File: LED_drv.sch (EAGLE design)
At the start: 42 parts, among them IC1 LM3409, IC2 LM393D, T1 IRLR9343PBF, T4 BT169, T5 BT169, T6 TLP266J

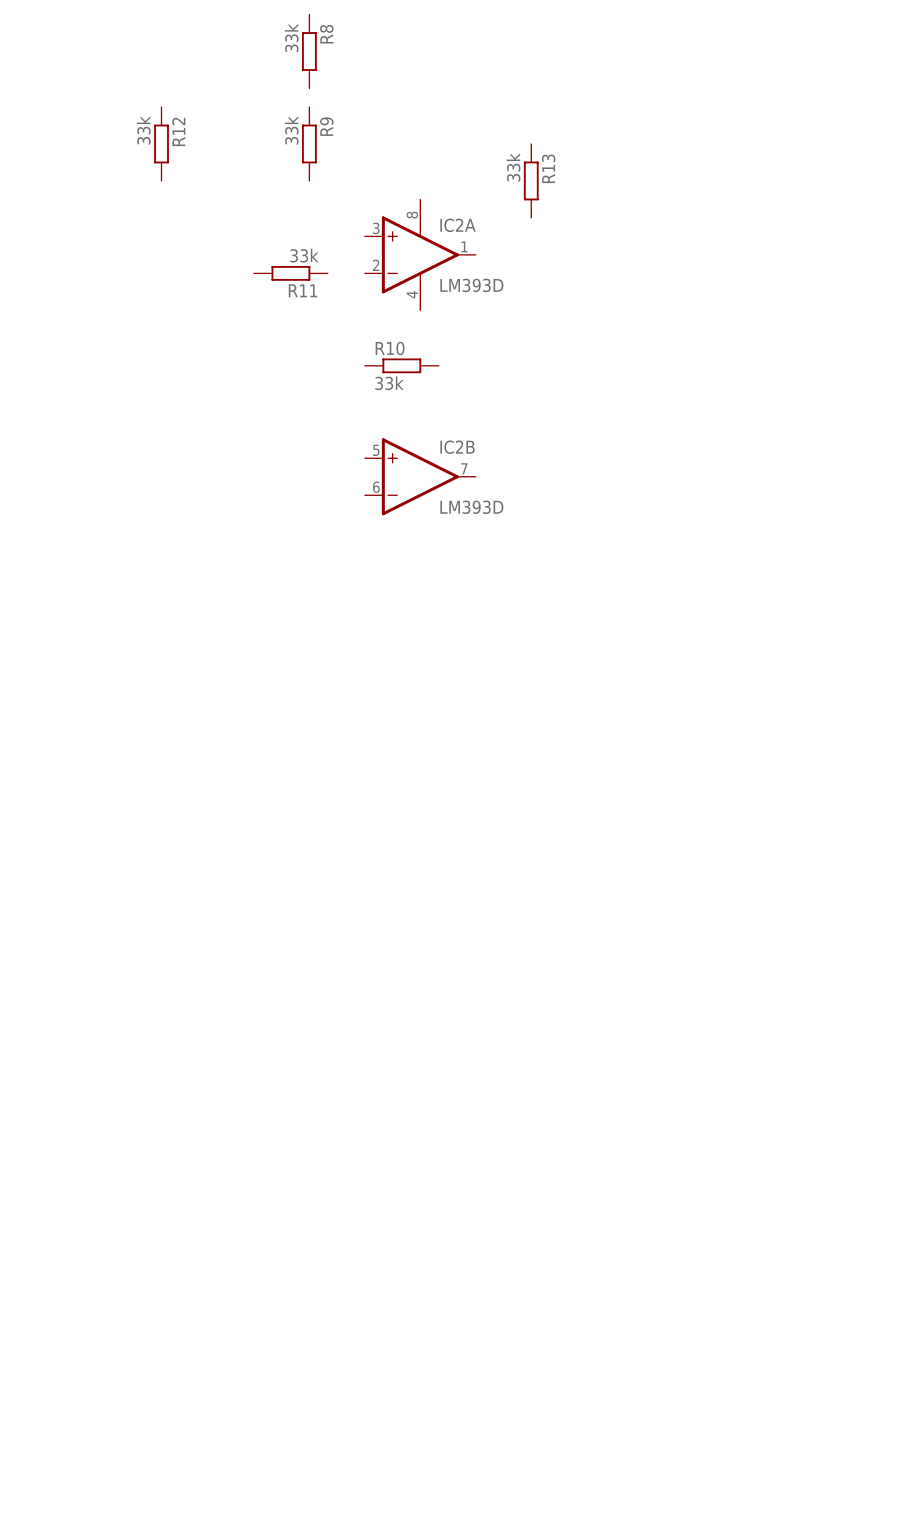
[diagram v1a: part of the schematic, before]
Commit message: Charge regeneration circuit
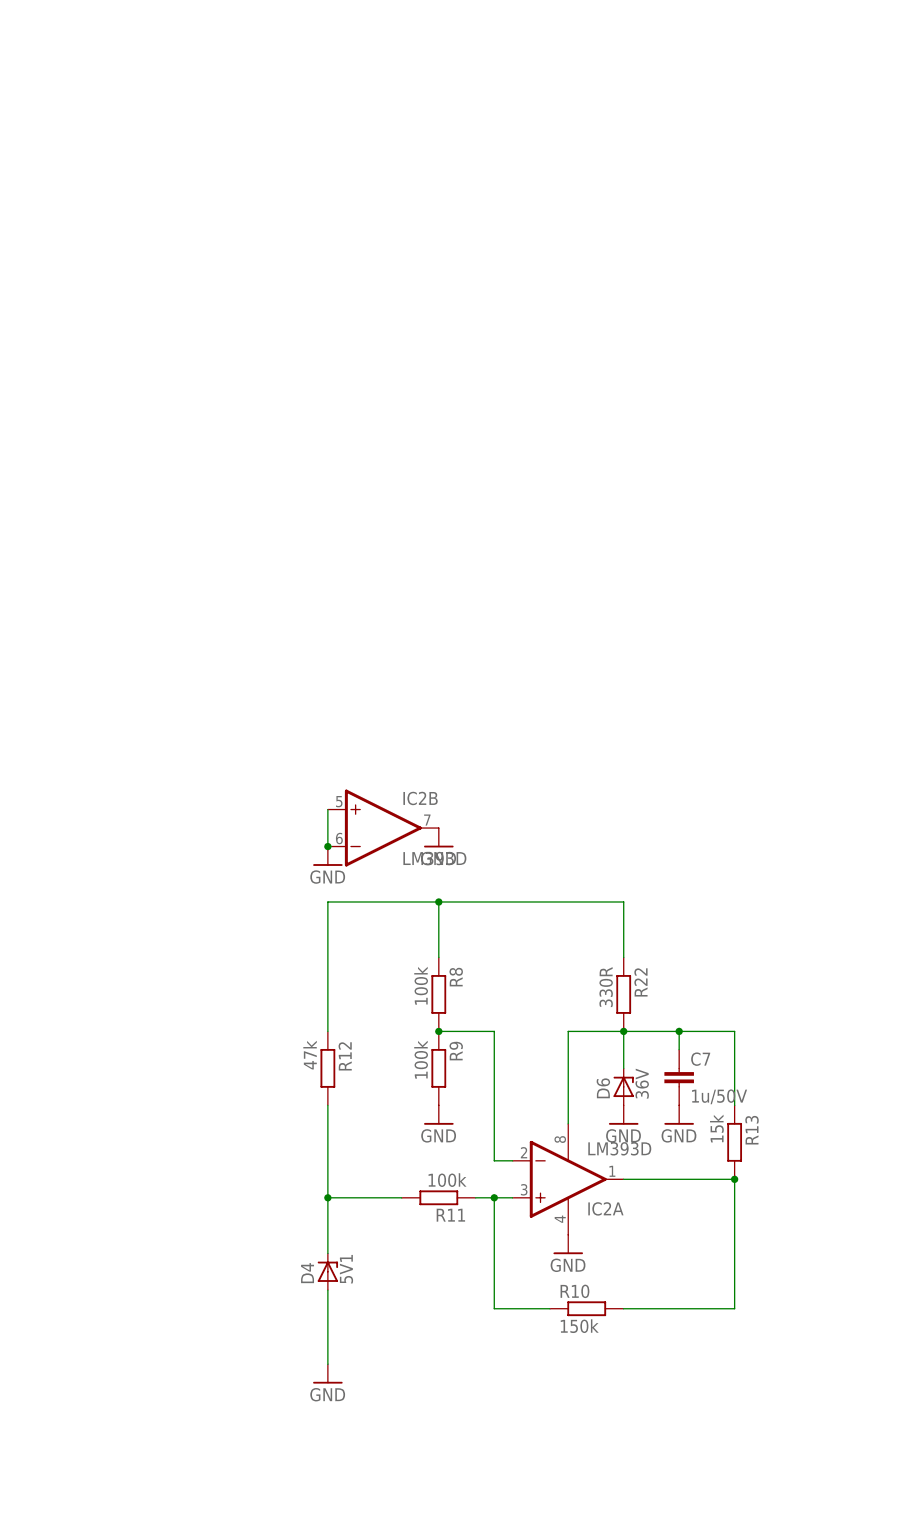
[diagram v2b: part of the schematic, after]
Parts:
- added C7: 1u/50V, rcl:C-EUC1206
- added D4: 5V1, diode:ZENER-DIODESOD80C
- added D6: 36V, diode:ZENER-DIODESOD80C
- added R22: 330R, resistor:R-EU_R0805
- R10: value 33k -> 150k
- R11, R8, R9: value 33k -> 100k
- R12: value 33k -> 47k
- R13: value 33k -> 15k
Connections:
- new net N$19: C7.1, D6.C, IC2P.V+, R13.1, R22.2
- new net N$20: IC2A.+IN, R10.1, R11.1
- new net N$21: IC2A.-IN, R8.2, R9.1
- new net N$22: D4.C, R11.2, R12.2
- new net N$27: R12.1, R22.1, R8.1
- new net N$29: IC2A.OUT, R10.2, R13.2
- net GND: now also C7.2, D4.A, D6.A, IC2B.+IN, IC2B.-IN, IC2B.OUT, IC2P.V-, R9.2
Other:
- moved on the sheet: IC2A, IC2B, R10, R11, R12, R13, R8, R9
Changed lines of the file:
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@@
 <setting verticaltext="up"/>
 </settings>
-<grid distance="0.1" unitdist="inch" unit="inch" style="lines" multiple="1" display="no" altdistance="0.05" altunitdist="inch" altunit="inch"/>
+<grid distance="0.1" unitdist="inch" unit="inch" style="lines" multiple="1" display="no" altdistance="0.01" altunitdist="inch" altunit="inch"/>
 <layers>
 <layer number="1" name="Top" color="4" fill="1" visible="no" active="no"/>
@@
 <part name="GND8" library="supply1" deviceset="GND" device=""/>
 <part name="IC2" library="linear" deviceset="LM393" device="D"/>
-<part name="R8" library="resistor" deviceset="R-EU_" device="R0805" value="33k"/>
-<part name="R9" library="resistor" deviceset="R-EU_" device="R0805" value="33k"/>
-<part name="R10" library="resistor" deviceset="R-EU_" device="R0805" value="33k"/>
-<part name="R11" library="resistor" deviceset="R-EU_" device="R0805" value="33k"/>
-<part name="R12" library="resistor" deviceset="R-EU_" device="R0805" value="33k"/>
-<part name="R13" library="resistor" deviceset="R-EU_" device="R0805" value="33k"/>
+<part name="R8" library="resistor" deviceset="R-EU_" device="R0805" value="100k"/>
+<part name="R9" library="resistor" deviceset="R-EU_" device="R0805" value="100k"/>
+<part name="R10" library="resistor" deviceset="R-EU_" device="R0805" value="150k"/>
+<part name="R11" library="resistor" deviceset="R-EU_" device="R0805" value="100k"/>
+<part name="R12" library="resistor" deviceset="R-EU_" device="R0805" value="47k"/>
 <part name="C6" library="rcl" deviceset="CPOL-US" device="E3.5-8" value="100n/400V"/>
 <part name="R17" library="rcl" deviceset="R-EU_" device="R1206" value="1M/200V"/>
@@
 <part name="R18" library="rcl" deviceset="R-EU_" device="R1206" value="700R"/>
 <part name="C8" library="rcl" deviceset="CPOL-US" device="E3.5-8" value="100u"/>
+<part name="GND9" library="supply1" deviceset="GND" device=""/>
+<part name="GND10" library="supply1" deviceset="GND" device=""/>
+<part name="D4" library="diode" deviceset="ZENER-DIODE" device="SOD80C" value="5V1"/>
+<part name="GND11" library="supply1" deviceset="GND" device=""/>
+<part name="D6" library="diode" deviceset="ZENER-DIODE" device="SOD80C" value="36V"/>
+<part name="R22" library="resistor" deviceset="R-EU_" device="R0805" value="330R"/>
+<part name="GND12" library="supply1" deviceset="GND" device=""/>
+<part name="C7" library="rcl" deviceset="C-EU" device="C1206" value="1u/50V"/>
+<part name="GND13" library="supply1" deviceset="GND" device=""/>
+<part name="GND14" library="supply1" deviceset="GND" device=""/>
+<part name="GND15" library="supply1" deviceset="GND" device=""/>
+<part name="R13" library="resistor" deviceset="R-EU_" device="R0805" value="15k"/>
 </parts>
 <sheets>
@@
 <instance part="R7" gate="G$1" x="2.54" y="-2.54" rot="R270"/>
 <instance part="GND8" gate="1" x="10.16" y="-7.62"/>
-<instance part="IC2" gate="A" x="236.22" y="119.38"/>
-<instance part="R8" gate="G$1" x="220.98" y="147.32" rot="R270"/>
-<instance part="R9" gate="G$1" x="220.98" y="134.62" rot="R270"/>
-<instance part="R10" gate="G$1" x="233.68" y="104.14"/>
-<instance part="R11" gate="G$1" x="218.44" y="116.84" rot="R180"/>
-<instance part="R12" gate="G$1" x="200.66" y="134.62" rot="R270"/>
-<instance part="R13" gate="G$1" x="251.46" y="129.54" rot="R270"/>
-<instance part="IC2" gate="P" x="236.22" y="119.38"/>
-<instance part="IC2" gate="B" x="236.22" y="88.9"/>
+<instance part="IC2" gate="A" x="256.54" y="-7.62" rot="MR180"/>
+<instance part="R8" gate="G$1" x="238.76" y="17.78" rot="R270"/>
+<instance part="R9" gate="G$1" x="238.76" y="7.62" rot="R270"/>
+<instance part="R10" gate="G$1" x="259.08" y="-25.4"/>
+<instance part="R11" gate="G$1" x="238.76" y="-10.16" rot="R180"/>
+<instance part="R12" gate="G$1" x="223.52" y="7.62" rot="R270"/>
+<instance part="IC2" gate="P" x="256.54" y="-7.62"/>
+<instance part="IC2" gate="B" x="231.14" y="40.64"/>
 <instance part="C6" gate="G$1" x="429.26" y="2.54"/>
 <instance part="R17" gate="G$1" x="429.26" y="-27.94" rot="R270"/>
@@
 <instance part="R18" gate="G$1" x="410.21" y="-53.34" rot="MR0"/>
 <instance part="C8" gate="G$1" x="411.48" y="-60.96" rot="R270"/>
+<instance part="GND9" gate="1" x="238.76" y="0"/>
+<instance part="GND10" gate="1" x="256.54" y="-17.78"/>
+<instance part="D4" gate="G$1" x="223.52" y="-20.32" rot="R90"/>
+<instance part="GND11" gate="1" x="223.52" y="-35.56"/>
+<instance part="D6" gate="G$1" x="264.16" y="5.08" rot="R90"/>
+<instance part="R22" gate="G$1" x="264.16" y="17.78" rot="R270"/>
+<instance part="GND12" gate="1" x="264.16" y="0"/>
+<instance part="C7" gate="G$1" x="271.78" y="7.62"/>
+<instance part="GND13" gate="1" x="271.78" y="0"/>
+<instance part="GND14" gate="1" x="223.52" y="35.56"/>
+<instance part="GND15" gate="1" x="238.76" y="38.1"/>
+<instance part="R13" gate="G$1" x="279.4" y="-2.54" rot="R270"/>
 </instances>
 <busses>
@@
 <pinref part="GND8" gate="1" pin="GND"/>
 </segment>
+<segment>
+<pinref part="R9" gate="G$1" pin="2"/>
+<pinref part="GND9" gate="1" pin="GND"/>
+</segment>
+<segment>
+<pinref part="IC2" gate="P" pin="V-"/>
+<pinref part="GND10" gate="1" pin="GND"/>
+</segment>
+<segment>
+<pinref part="D4" gate="G$1" pin="A"/>
+<wire x1="223.52" y1="-22.86" x2="223.52" y2="-33.02" width="0.1524" layer="91"/>
+<pinref part="GND11" gate="1" pin="GND"/>
+</segment>
+<segment>
+<pinref part="D6" gate="G$1" pin="A"/>
+<pinref part="GND12" gate="1" pin="GND"/>
+</segment>
+<segment>
+<pinref part="C7" gate="G$1" pin="2"/>
+<pinref part="GND13" gate="1" pin="GND"/>
+</segment>
+<segment>
+<pinref part="IC2" gate="B" pin="-IN"/>
+<pinref part="GND14" gate="1" pin="GND"/>
+<pinref part="IC2" gate="B" pin="+IN"/>
+<wire x1="223.52" y1="43.18" x2="223.52" y2="38.1" width="0.1524" layer="91"/>
+<junction x="223.52" y="38.1"/>
+</segment>
+<segment>
+<pinref part="IC2" gate="B" pin="OUT"/>
+<pinref part="GND15" gate="1" pin="GND"/>
+</segment>
 </net>
 <net name="N$4" class="0">
@@
 </segment>
 </net>
+<net name="N$20" class="0">
+<segment>
+<pinref part="R10" gate="G$1" pin="1"/>
+<wire x1="254" y1="-25.4" x2="246.38" y2="-25.4" width="0.1524" layer="91"/>
+<wire x1="246.38" y1="-25.4" x2="246.38" y2="-10.16" width="0.1524" layer="91"/>
+<pinref part="R11" gate="G$1" pin="1"/>
+<wire x1="246.38" y1="-10.16" x2="243.84" y2="-10.16" width="0.1524" layer="91"/>
+<pinref part="IC2" gate="A" pin="+IN"/>
+<wire x1="248.92" y1="-10.16" x2="246.38" y2="-10.16" width="0.1524" layer="91"/>
+<junction x="246.38" y="-10.16"/>
+</segment>
+</net>
+<net name="N$21" class="0">
+<segment>
+<pinref part="R8" gate="G$1" pin="2"/>
+<pinref part="R9" gate="G$1" pin="1"/>
+<wire x1="238.76" y1="12.7" x2="246.38" y2="12.7" width="0.1524" layer="91"/>
+<wire x1="246.38" y1="12.7" x2="246.38" y2="-5.08" width="0.1524" layer="91"/>
+<junction x="238.76" y="12.7"/>
+<pinref part="IC2" gate="A" pin="-IN"/>
+<wire x1="246.38" y1="-5.08" x2="248.92" y2="-5.08" width="0.1524" layer="91"/>
+</segment>
+</net>
+<net name="N$22" class="0">
+<segment>
+<pinref part="R11" gate="G$1" pin="2"/>
+<pinref part="R12" gate="G$1" pin="2"/>
+<wire x1="233.68" y1="-10.16" x2="223.52" y2="-10.16" width="0.1524" layer="91"/>
+<wire x1="223.52" y1="-10.16" x2="223.52" y2="2.54" width="0.1524" layer="91"/>
+<pinref part="D4" gate="G$1" pin="C"/>
+<wire x1="223.52" y1="-17.78" x2="223.52" y2="-10.16" width="0.1524" layer="91"/>
+<junction x="223.52" y="-10.16"/>
+</segment>
+</net>
+<net name="N$27" class="0">
+<segment>
+<pinref part="R12" gate="G$1" pin="1"/>
+<wire x1="223.52" y1="12.7" x2="223.52" y2="30.48" width="0.1524" layer="91"/>
+<wire x1="223.52" y1="30.48" x2="238.76" y2="30.48" width="0.1524" layer="91"/>
+<wire x1="238.76" y1="30.48" x2="264.16" y2="30.48" width="0.1524" layer="91"/>
+<pinref part="R8" gate="G$1" pin="1"/>
+<wire x1="238.76" y1="22.86" x2="238.76" y2="30.48" width="0.1524" layer="91"/>
+<junction x="238.76" y="30.48"/>
+<pinref part="R22" gate="G$1" pin="1"/>
+<wire x1="264.16" y1="22.86" x2="264.16" y2="30.48" width="0.1524" layer="91"/>
+</segment>
+</net>
+<net name="N$29" class="0">
+<segment>
+<pinref part="R10" gate="G$1" pin="2"/>
+<wire x1="264.16" y1="-25.4" x2="279.4" y2="-25.4" width="0.1524" layer="91"/>
+<wire x1="279.4" y1="-25.4" x2="279.4" y2="-7.62" width="0.1524" layer="91"/>
+<pinref part="IC2" gate="A" pin="OUT"/>
+<wire x1="264.16" y1="-7.62" x2="279.4" y2="-7.62" width="0.1524" layer="91"/>
+<pinref part="R13" gate="G$1" pin="2"/>
+<junction x="279.4" y="-7.62"/>
+</segment>
+</net>
+<net name="N$19" class="0">
+<segment>
+<wire x1="271.78" y1="12.7" x2="279.4" y2="12.7" width="0.1524" layer="91"/>
+<pinref part="C7" gate="G$1" pin="1"/>
+<wire x1="271.78" y1="10.16" x2="271.78" y2="12.7" width="0.1524" layer="91"/>
+<junction x="271.78" y="12.7"/>
+<pinref part="D6" gate="G$1" pin="C"/>
+<pinref part="R22" gate="G$1" pin="2"/>
+<wire x1="264.16" y1="12.7" x2="264.16" y2="7.62" width="0.1524" layer="91"/>
+<wire x1="264.16" y1="12.7" x2="271.78" y2="12.7" width="0.1524" layer="91"/>
+<junction x="264.16" y="12.7"/>
+<wire x1="256.54" y1="12.7" x2="264.16" y2="12.7" width="0.1524" layer="91"/>
+<pinref part="IC2" gate="P" pin="V+"/>
+<wire x1="256.54" y1="0" x2="256.54" y2="12.7" width="0.1524" layer="91"/>
+<pinref part="R13" gate="G$1" pin="1"/>
+<wire x1="279.4" y1="2.54" x2="279.4" y2="12.7" width="0.1524" layer="91"/>
+</segment>
+</net>
